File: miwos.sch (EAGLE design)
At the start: 47 parts

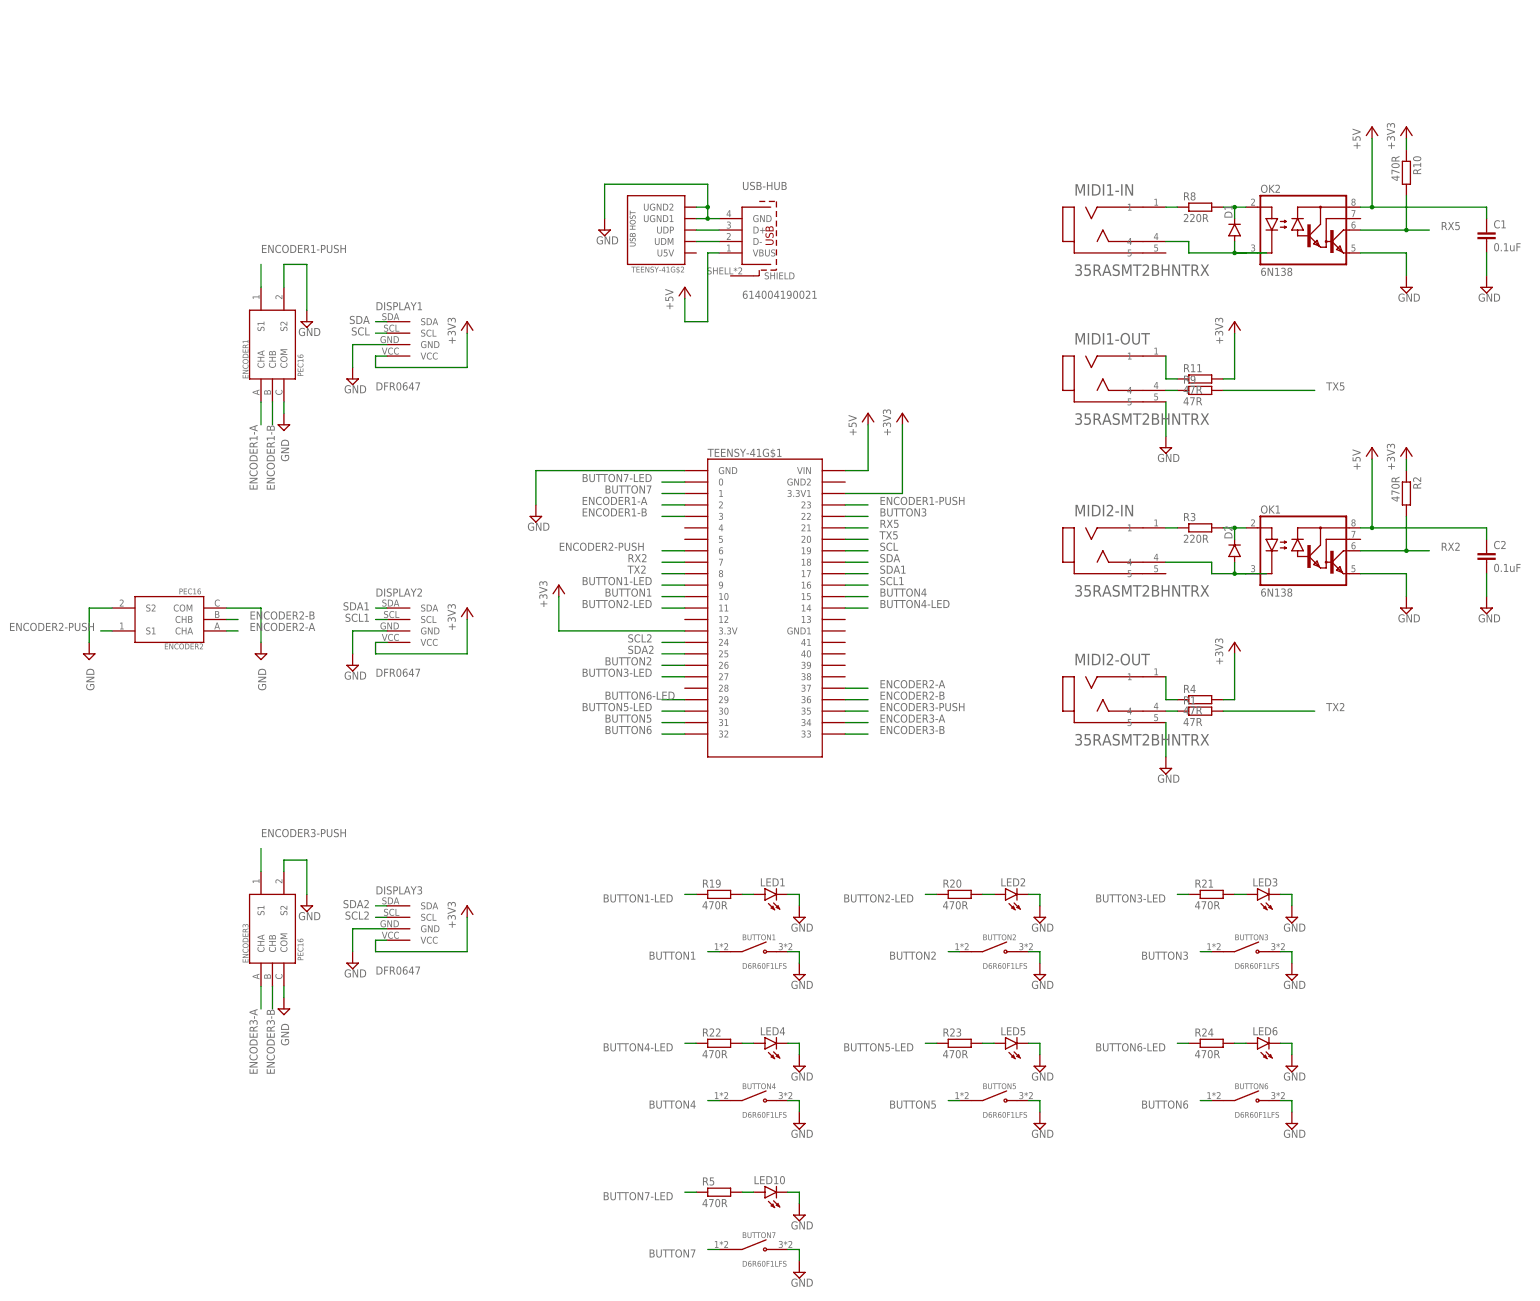
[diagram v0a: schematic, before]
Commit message: Various changes, add mounting holes
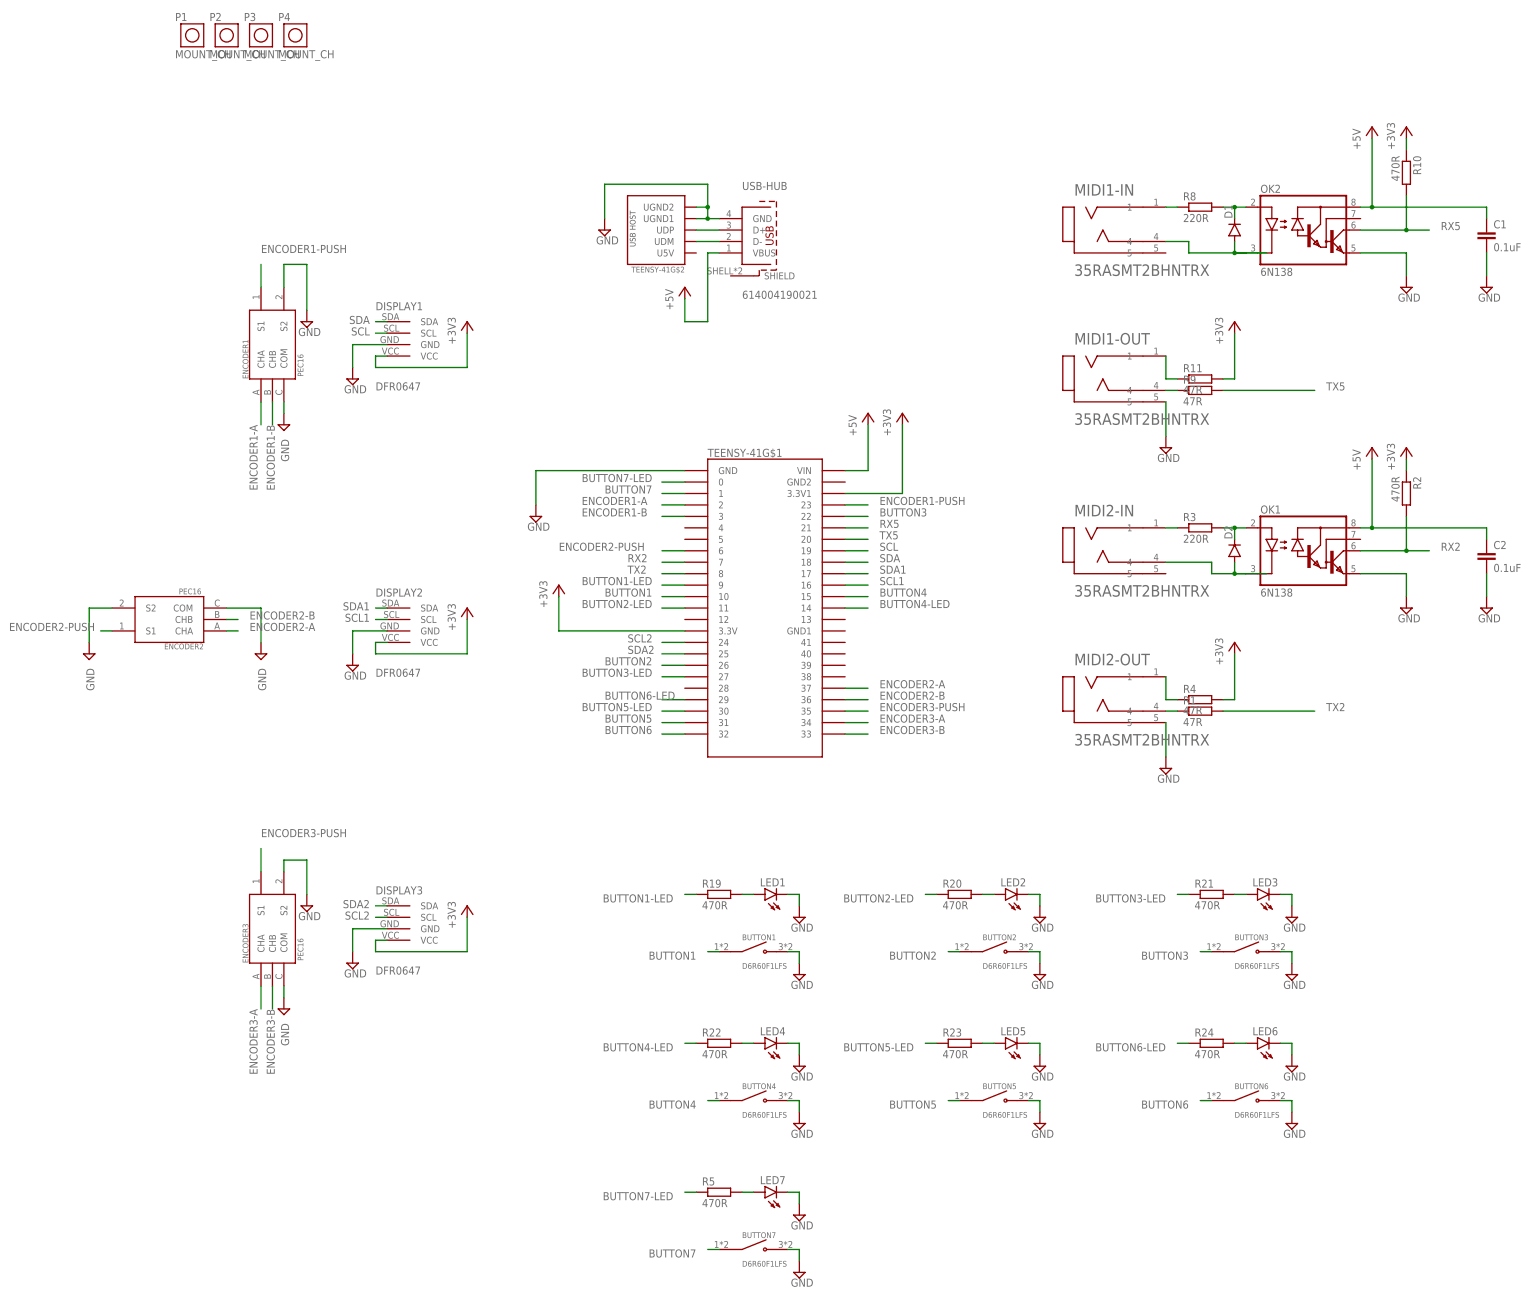
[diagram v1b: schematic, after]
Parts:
- added P1, P2, P3, P4: MOUNT_CH, sol_pin:MOUNT_CH
- renumbered LED10 to LED7
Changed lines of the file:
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@@
 <drawing>
 <settings>
-<setting alwaysvectorfont="yes"/>
+<setting alwaysvectorfont="no"/>
 <setting verticaltext="up"/>
 </settings>
@@
 <part name="SUPPLY11" library="supply2" library_urn="urn:adsk.eagle:library:372" deviceset="GND" device=""/>
 <part name="R5" library="rcl" library_urn="urn:adsk.eagle:library:334" deviceset="R-EU_" device="R0603" package3d_urn="urn:adsk.eagle:package:23555/3" value="470R"/>
-<part name="LED10" library="led" library_urn="urn:adsk.eagle:library:259" deviceset="LED" device="3MM" package3d_urn="urn:adsk.eagle:package:15797/1"/>
+<part name="LED7" library="led" library_urn="urn:adsk.eagle:library:259" deviceset="LED" device="3MM" package3d_urn="urn:adsk.eagle:package:15797/1"/>
 <part name="MIDI1-IN" library="35RASMT2BHNTRX" deviceset="35RASMT2BHNTRX" device=""/>
 <part name="MIDI1-OUT" library="35RASMT2BHNTRX" deviceset="35RASMT2BHNTRX" device=""/>
@@
 <part name="SUPPLY3" library="supply2" library_urn="urn:adsk.eagle:library:372" deviceset="GND" device=""/>
 <part name="SUPPLY4" library="supply2" library_urn="urn:adsk.eagle:library:372" deviceset="GND" device=""/>
+<part name="P1" library="sol_pin" deviceset="MOUNT_CH" device=""/>
+<part name="P2" library="sol_pin" deviceset="MOUNT_CH" device=""/>
+<part name="P3" library="sol_pin" deviceset="MOUNT_CH" device=""/>
+<part name="P4" library="sol_pin" deviceset="MOUNT_CH" device=""/>
 </parts>
 <sheets>
@@
 <attribute name="VALUE" x="11.43" y="-71.882" size="1.778" layer="96"/>
 </instance>
-<instance part="LED10" gate="G$1" x="25.4" y="-68.58" smashed="yes" rot="R90">
+<instance part="LED7" gate="G$1" x="25.4" y="-68.58" smashed="yes" rot="R90">
 <attribute name="NAME" x="29.972" y="-65.024" size="1.778" layer="95" rot="R180"/>
 <attribute name="VALUE" x="29.972" y="-62.865" size="1.778" layer="96" rot="R180"/>
@@
 <instance part="SUPPLY4" gate="GND" x="-86.36" y="50.8" smashed="yes">
 <attribute name="VALUE" x="-86.995" y="47.625" size="1.778" layer="96" rot="R270"/>
+</instance>
+<instance part="P1" gate="G$1" x="-101.6" y="187.96" smashed="yes">
+<attribute name="NAME" x="-105.41" y="191.135" size="1.778" layer="95"/>
+<attribute name="VALUE" x="-105.41" y="182.88" size="1.778" layer="96"/>
+</instance>
+<instance part="P2" gate="G$1" x="-93.98" y="187.96" smashed="yes">
+<attribute name="NAME" x="-97.79" y="191.135" size="1.778" layer="95"/>
+<attribute name="VALUE" x="-97.79" y="182.88" size="1.778" layer="96"/>
+</instance>
+<instance part="P3" gate="G$1" x="-86.36" y="187.96" smashed="yes">
+<attribute name="NAME" x="-90.17" y="191.135" size="1.778" layer="95"/>
+<attribute name="VALUE" x="-90.17" y="182.88" size="1.778" layer="96"/>
+</instance>
+<instance part="P4" gate="G$1" x="-78.74" y="187.96" smashed="yes">
+<attribute name="NAME" x="-82.55" y="191.135" size="1.778" layer="95"/>
+<attribute name="VALUE" x="-82.55" y="182.88" size="1.778" layer="96"/>
 </instance>
 </instances>
@@
 <wire x1="30.48" y1="-68.58" x2="33.02" y2="-68.58" width="0.1524" layer="91"/>
 <wire x1="33.02" y1="-68.58" x2="33.02" y2="-71.12" width="0.1524" layer="91"/>
-<pinref part="LED10" gate="G$1" pin="C"/>
+<pinref part="LED7" gate="G$1" pin="C"/>
 </segment>
 <segment>
@@
 <wire x1="22.86" y1="-68.58" x2="20.32" y2="-68.58" width="0.1524" layer="91"/>
 <pinref part="R5" gate="G$1" pin="2"/>
-<pinref part="LED10" gate="G$1" pin="A"/>
-</segment>
-</net>
+<pinref part="LED7" gate="G$1" pin="A"/>
+</segment>
+</net>

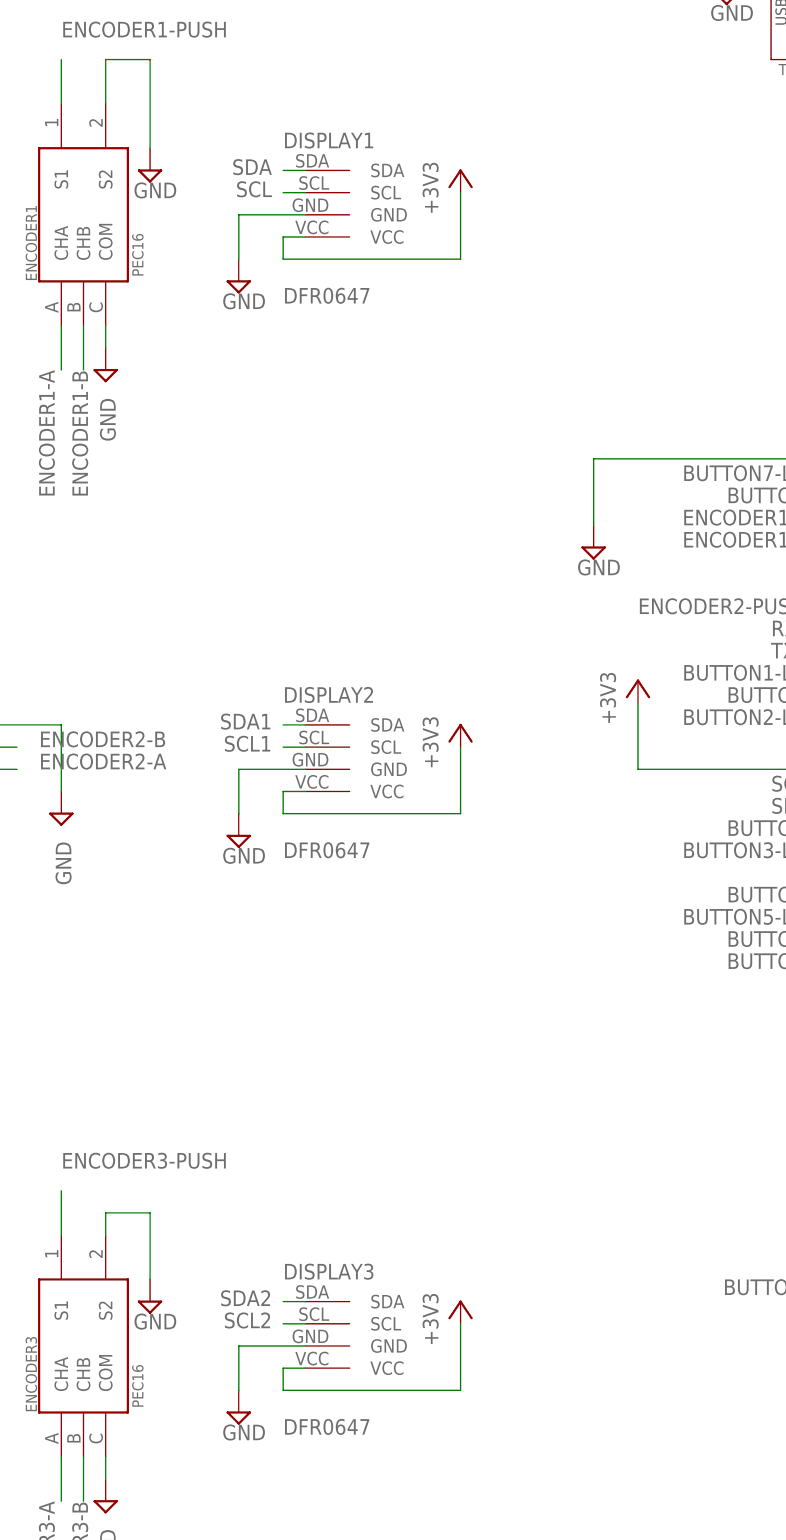
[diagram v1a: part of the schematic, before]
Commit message: Rotate LEDs
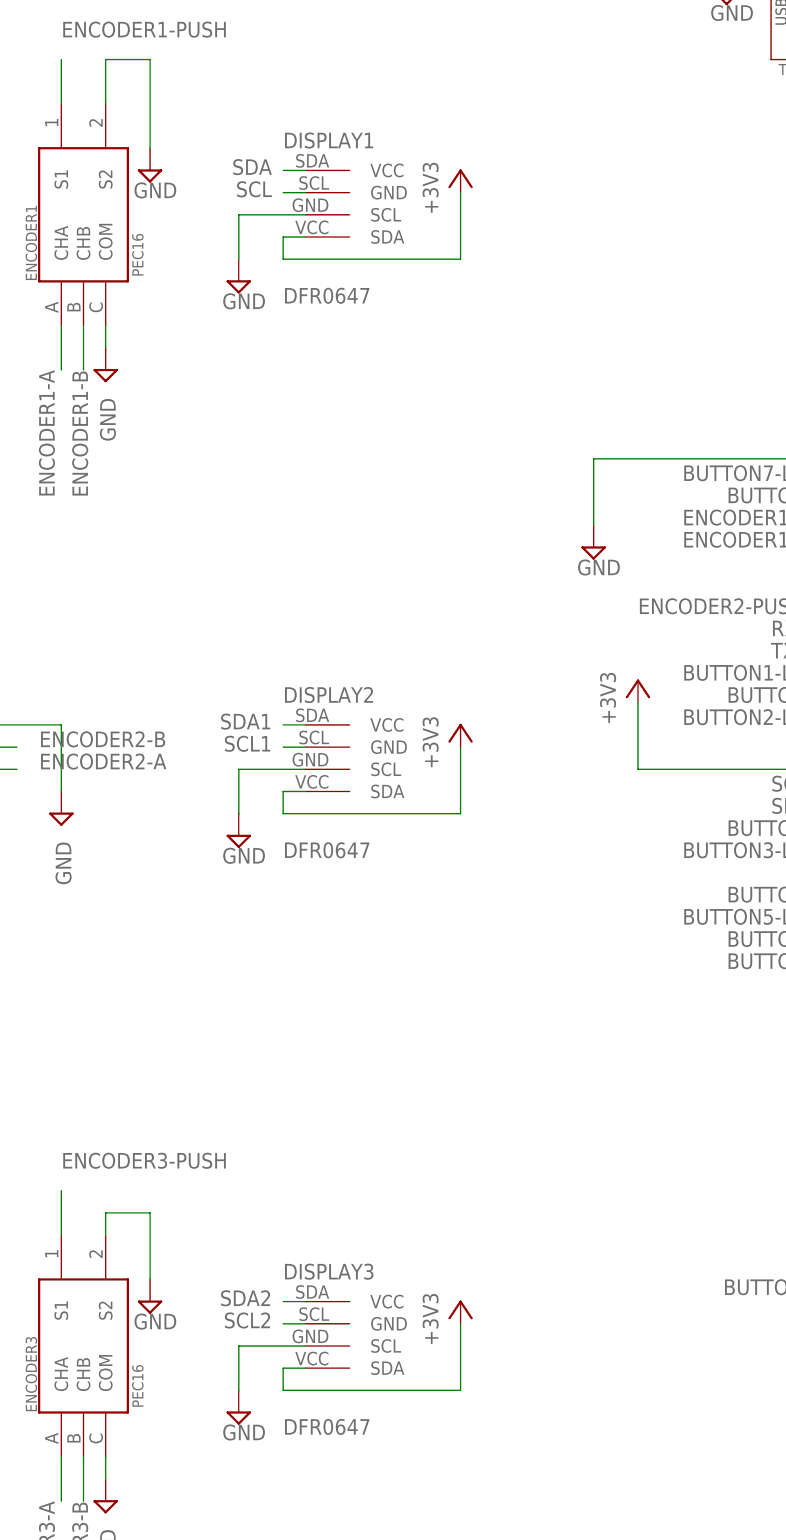
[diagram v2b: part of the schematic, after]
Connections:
- net +3V3: now also DISPLAY1.SDA, DISPLAY2.SDA, DISPLAY3.SDA; no longer DISPLAY1.VCC, DISPLAY2.VCC, DISPLAY3.VCC
- net GND: now also DISPLAY1.SCL, DISPLAY2.SCL, DISPLAY3.SCL; no longer DISPLAY1.GND, DISPLAY2.GND, DISPLAY3.GND
- net SCL: now also DISPLAY1.GND; no longer DISPLAY1.SCL
- net SCL1: now also DISPLAY2.GND; no longer DISPLAY2.SCL
- net SCL2: now also DISPLAY3.GND; no longer DISPLAY3.SCL
- net SDA: now also DISPLAY1.VCC; no longer DISPLAY1.SDA
- net SDA1: now also DISPLAY2.VCC; no longer DISPLAY2.SDA
- net SDA2: now also DISPLAY3.VCC; no longer DISPLAY3.SDA
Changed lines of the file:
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@@
 <drawing>
 <settings>
-<setting alwaysvectorfont="no"/>
+<setting alwaysvectorfont="yes"/>
 <setting verticaltext="up"/>
 </settings>
@@
 </segment>
 <segment>
-<pinref part="DISPLAY1" gate="G$1" pin="GND"/>
+<pinref part="DISPLAY1" gate="G$1" pin="SCL"/>
 <wire x1="-58.42" y1="119.38" x2="-66.04" y2="119.38" width="0.1524" layer="91"/>
 <pinref part="SUPPLY33" gate="GND" pin="GND"/>
@@
 </segment>
 <segment>
-<pinref part="DISPLAY2" gate="G$1" pin="GND"/>
+<pinref part="DISPLAY2" gate="G$1" pin="SCL"/>
 <wire x1="-58.42" y1="55.88" x2="-66.04" y2="55.88" width="0.1524" layer="91"/>
 <pinref part="SUPPLY34" gate="GND" pin="GND"/>
@@
 </segment>
 <segment>
-<pinref part="DISPLAY3" gate="G$1" pin="GND"/>
+<pinref part="DISPLAY3" gate="G$1" pin="SCL"/>
 <wire x1="-58.42" y1="-10.16" x2="-66.04" y2="-10.16" width="0.1524" layer="91"/>
 <pinref part="SUPPLY35" gate="GND" pin="GND"/>
@@
 </segment>
 <segment>
-<pinref part="DISPLAY1" gate="G$1" pin="VCC"/>
+<pinref part="DISPLAY1" gate="G$1" pin="SDA"/>
 <wire x1="-58.42" y1="116.84" x2="-60.96" y2="116.84" width="0.1524" layer="91"/>
 <wire x1="-60.96" y1="116.84" x2="-60.96" y2="114.3" width="0.1524" layer="91"/>
@@
 </segment>
 <segment>
-<pinref part="DISPLAY2" gate="G$1" pin="VCC"/>
+<pinref part="DISPLAY2" gate="G$1" pin="SDA"/>
 <wire x1="-58.42" y1="53.34" x2="-60.96" y2="53.34" width="0.1524" layer="91"/>
 <wire x1="-60.96" y1="53.34" x2="-60.96" y2="50.8" width="0.1524" layer="91"/>
@@
 </segment>
 <segment>
-<pinref part="DISPLAY3" gate="G$1" pin="VCC"/>
+<pinref part="DISPLAY3" gate="G$1" pin="SDA"/>
 <wire x1="-58.42" y1="-12.7" x2="-60.96" y2="-12.7" width="0.1524" layer="91"/>
 <wire x1="-60.96" y1="-12.7" x2="-60.96" y2="-15.24" width="0.1524" layer="91"/>
@@
 </segment>
 <segment>
-<pinref part="DISPLAY1" gate="G$1" pin="SDA"/>
+<pinref part="DISPLAY1" gate="G$1" pin="VCC"/>
 <wire x1="-58.42" y1="124.46" x2="-60.96" y2="124.46" width="0.1524" layer="91"/>
 <label x="-62.23" y="125.73" size="1.778" layer="95" rot="R180"/>
@@
 </segment>
 <segment>
-<pinref part="DISPLAY2" gate="G$1" pin="SDA"/>
+<pinref part="DISPLAY2" gate="G$1" pin="VCC"/>
 <wire x1="-58.42" y1="60.96" x2="-60.96" y2="60.96" width="0.1524" layer="91"/>
 <label x="-62.23" y="62.23" size="1.778" layer="95" rot="R180"/>
@@
 </segment>
 <segment>
-<pinref part="DISPLAY3" gate="G$1" pin="SDA"/>
+<pinref part="DISPLAY3" gate="G$1" pin="VCC"/>
 <wire x1="-58.42" y1="-5.08" x2="-60.96" y2="-5.08" width="0.1524" layer="91"/>
 <label x="-62.23" y="-3.81" size="1.778" layer="95" rot="R180"/>
@@
 </segment>
 <segment>
-<pinref part="DISPLAY1" gate="G$1" pin="SCL"/>
+<pinref part="DISPLAY1" gate="G$1" pin="GND"/>
 <wire x1="-58.42" y1="121.92" x2="-60.96" y2="121.92" width="0.1524" layer="91"/>
 <label x="-62.23" y="123.19" size="1.778" layer="95" rot="R180"/>
@@
 </segment>
 <segment>
-<pinref part="DISPLAY2" gate="G$1" pin="SCL"/>
+<pinref part="DISPLAY2" gate="G$1" pin="GND"/>
 <wire x1="-58.42" y1="58.42" x2="-60.96" y2="58.42" width="0.1524" layer="91"/>
 <label x="-62.23" y="59.69" size="1.778" layer="95" rot="R180"/>
@@
 </segment>
 <segment>
-<pinref part="DISPLAY3" gate="G$1" pin="SCL"/>
+<pinref part="DISPLAY3" gate="G$1" pin="GND"/>
 <wire x1="-58.42" y1="-7.62" x2="-60.96" y2="-7.62" width="0.1524" layer="91"/>
 <label x="-62.23" y="-6.35" size="1.778" layer="95" rot="R180"/>
